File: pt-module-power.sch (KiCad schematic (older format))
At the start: 21 parts, among them U1 MCP16331, U2 MCP16331

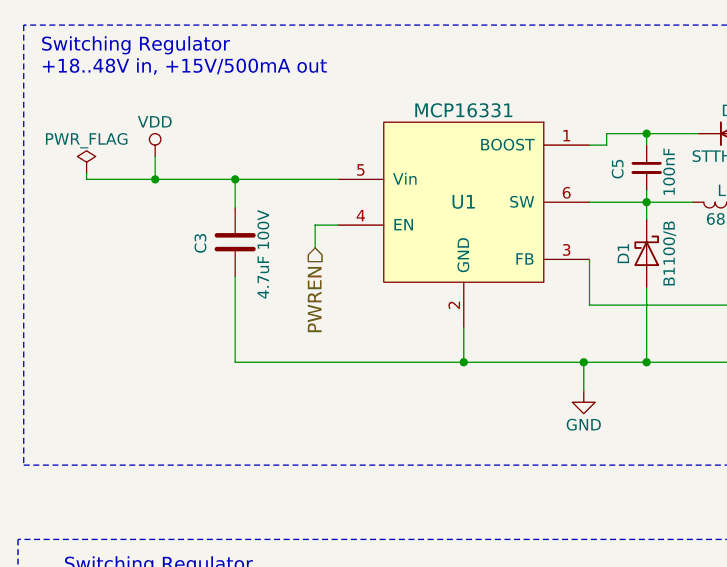
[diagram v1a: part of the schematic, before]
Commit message: Delete pwren
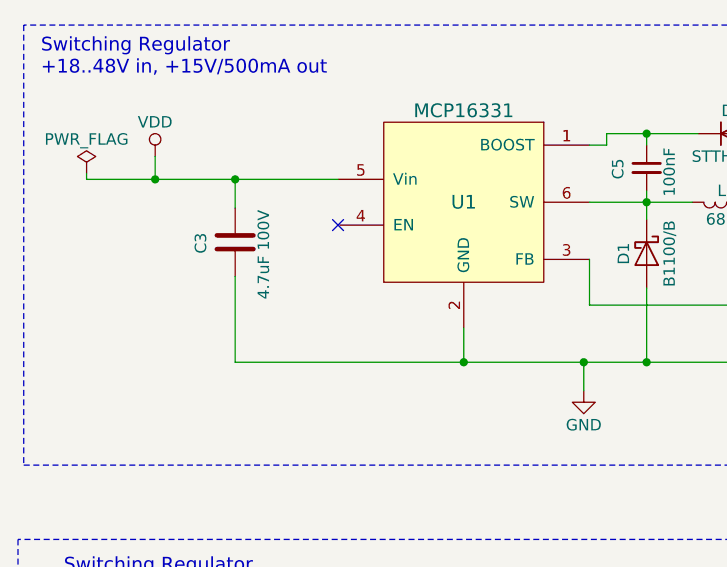
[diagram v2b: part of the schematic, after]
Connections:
- net PWREN: no longer names the net of U1.4 (EN)
- no-connect marks 1 -> 2
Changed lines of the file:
@@
 $EndComp
 $Comp
-L VCC #PWR17
+L VCC #PWR018
 U 1 1 598C3307
 P 3600 4400
-F 0 "#PWR17" H 3600 4250 50  0001 C CNN
+F 0 "#PWR018" H 3600 4250 50  0001 C CNN
 F 1 "VCC" H 3600 4550 50  0000 C CNN
 F 2 "" H 3600 4400 50  0001 C CNN
@@
 $EndComp
 $Comp
-L GND #PWR20
+L GND #PWR019
 U 1 1 598C36A8
 P 4050 4700
-F 0 "#PWR20" H 4050 4450 50  0001 C CNN
+F 0 "#PWR019" H 4050 4450 50  0001 C CNN
 F 1 "GND" H 4050 4550 50  0000 C CNN
 F 2 "" H 4050 4700 50  0001 C CNN
@@
 $EndComp
 $Comp
-L GND #PWR21
+L GND #PWR020
 U 1 1 598C3B7E
 P 5250 5050
-F 0 "#PWR21" H 5250 4800 50  0001 C CNN
+F 0 "#PWR020" H 5250 4800 50  0001 C CNN
 F 1 "GND" H 5250 4900 50  0000 C CNN
 F 2 "" H 5250 5050 50  0001 C CNN
@@
 $EndComp
 $Comp
-L GND #PWR24
+L GND #PWR021
 U 1 1 598C3C64
 P 6550 5500
-F 0 "#PWR24" H 6550 5250 50  0001 C CNN
+F 0 "#PWR021" H 6550 5250 50  0001 C CNN
 F 1 "GND" H 6550 5350 50  0000 C CNN
 F 2 "" H 6550 5500 50  0001 C CNN
@@
 $EndComp
 $Comp
-L GND #PWR23
+L GND #PWR022
 U 1 1 598C5043
 P 6250 4800
-F 0 "#PWR23" H 6250 4550 50  0001 C CNN
+F 0 "#PWR022" H 6250 4550 50  0001 C CNN
 F 1 "GND" H 6250 4650 50  0000 C CNN
 F 2 "" H 6250 4800 50  0001 C CNN
@@
 $EndComp
 $Comp
-L +3.3V #PWR27
+L +3.3V #PWR023
 U 1 1 598C94DC
 P 7500 4600
-F 0 "#PWR27" H 7500 4450 50  0001 C CNN
+F 0 "#PWR023" H 7500 4450 50  0001 C CNN
 F 1 "+3.3V" H 7500 4740 50  0000 C CNN
 F 2 "" H 7500 4600 50  0001 C CNN
@@
 $EndComp
 $Comp
-L PWR_FLAG #FLG5
+L PWR_FLAG #FLG024
 U 1 1 598C9528
 P 7750 4850
-F 0 "#FLG5" H 7750 4925 50  0001 C CNN
+F 0 "#FLG024" H 7750 4925 50  0001 C CNN
 F 1 "PWR_FLAG" H 7750 5000 50  0000 C CNN
 F 2 "" H 7750 4850 50  0001 C CNN
@@
 $EndComp
 $Comp
-L GND #PWR25
+L GND #PWR025
 U 1 1 598CA371
 P 6900 5150
-F 0 "#PWR25" H 6900 4900 50  0001 C CNN
+F 0 "#PWR025" H 6900 4900 50  0001 C CNN
 F 1 "GND" H 6900 5000 50  0000 C CNN
 F 2 "" H 6900 5150 50  0001 C CNN
@@
 $EndComp
 $Comp
-L GND #PWR18
+L GND #PWR026
 U 1 1 598CEACF
 P 3700 4700
-F 0 "#PWR18" H 3700 4450 50  0001 C CNN
+F 0 "#PWR026" H 3700 4450 50  0001 C CNN
 F 1 "GND" H 3700 4550 50  0000 C CNN
 F 2 "" H 3700 4700 50  0001 C CNN
@@
 $EndComp
 $Comp
-L GND #PWR26
+L GND #PWR027
 U 1 1 598CEF8A
 P 7350 5150
-F 0 "#PWR26" H 7350 4900 50  0001 C CNN
+F 0 "#PWR027" H 7350 4900 50  0001 C CNN
 F 1 "GND" H 7350 5000 50  0000 C CNN
 F 2 "" H 7350 5150 50  0001 C CNN
@@
 External_VCC
 $Comp
-L PWR_FLAG #FLG4
+L PWR_FLAG #FLG028
 U 1 1 597BEB38
 P 7725 2225
-F 0 "#FLG4" H 7725 2300 50  0001 C CNN
+F 0 "#FLG028" H 7725 2300 50  0001 C CNN
 F 1 "PWR_FLAG" H 7725 2375 50  0000 C CNN
 F 2 "" H 7725 2225 50  0001 C CNN
@@
 $EndComp
 $Comp
-L GND #PWR22
+L GND #PWR029
 U 1 1 597A23E8
 P 5675 3100
-F 0 "#PWR22" H 5675 2850 50  0001 C CNN
+F 0 "#PWR029" H 5675 2850 50  0001 C CNN
 F 1 "GND" H 5675 2950 50  0000 C CNN
 F 2 "" H 5675 3100 50  0001 C CNN
@@
 	0    1    1    0
 $EndComp
-Wire Wire Line
-	4500 2375 4600 2375
-Wire Wire Line
-	4500 2475 4500 2375
 Wire Notes Line
 	8025 1500 3225 1500
@@
 Text Notes 3300 1725 0    60   ~ 0
 Switching Regulator\n+18..48V in, +15V/500mA out
-Text HLabel 4500 2475 3    60   Input ~ 0
-PWREN
 $Comp
 L MCP16331 U1
@@
 $EndComp
 $Comp
-L VDD #PWR19
+L VDD #PWR030
 U 1 1 597A11B1
 P 3800 2075
-F 0 "#PWR19" H 3800 1925 50  0001 C CNN
+F 0 "#PWR030" H 3800 1925 50  0001 C CNN
 F 1 "VDD" H 3800 2225 50  0000 C CNN
 F 2 "" H 3800 2075 50  0001 C CNN
@@
 $EndComp
 $Comp
-L PWR_FLAG #FLG3
+L PWR_FLAG #FLG031
 U 1 1 59948AC3
 P 3500 2150
-F 0 "#FLG3" H 3500 2225 50  0001 C CNN
+F 0 "#FLG031" H 3500 2225 50  0001 C CNN
 F 1 "PWR_FLAG" H 3500 2300 50  0000 C CNN
 F 2 "" H 3500 2150 50  0001 C CNN
@@
 Connection ~ 3800 2175
 $Comp
-L PWR_FLAG #FLG2
+L PWR_FLAG #FLG032
 U 1 1 59958159
 P 3475 4400
-F 0 "#FLG2" H 3475 4475 50  0001 C CNN
+F 0 "#FLG032" H 3475 4475 50  0001 C CNN
 F 1 "PWR_FLAG" H 3475 4550 50  0000 C CNN
 F 2 "" H 3475 4400 50  0001 C CNN
@@
 $EndComp
 Connection ~ 3600 4400
+NoConn ~ 4600 2375
 $EndSCHEMATC

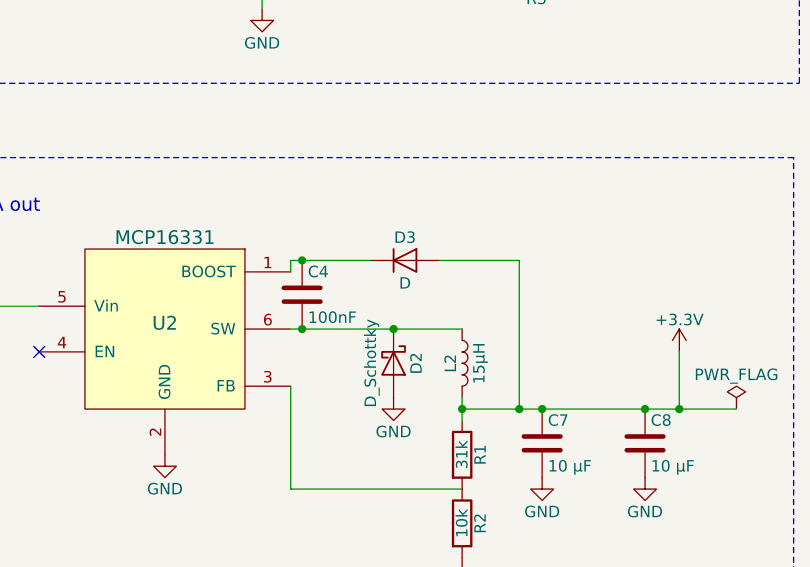
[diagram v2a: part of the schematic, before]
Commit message: add all the rest of the footprints
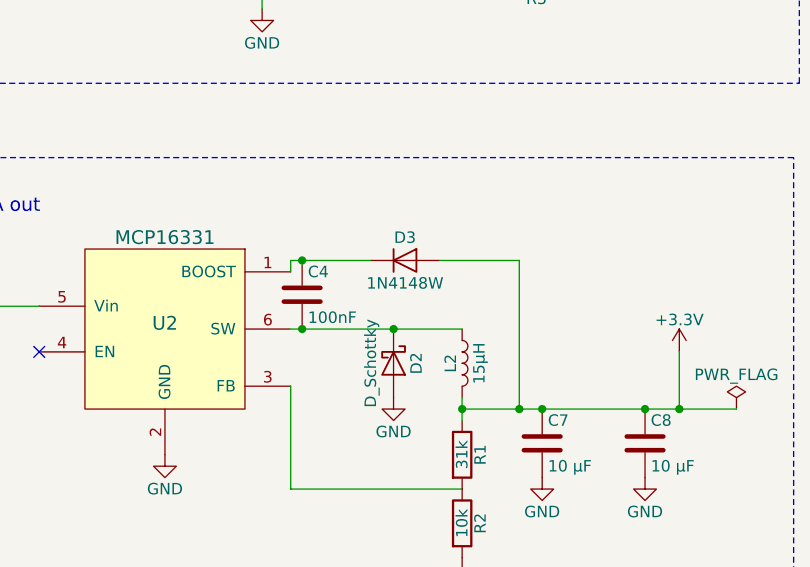
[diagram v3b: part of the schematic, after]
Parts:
- C1, C2, C3, C4, C5, C6, C7, C8: footprint (none) -> Capacitors_SMD:C_1206_HandSoldering
- D2: footprint (none) -> Diodes_SMD:D_SMA
- D3: value D -> 1N4148W; footprint (none) -> Diodes_SMD:D_SOD-123F
- L2: footprint (none) -> .pretty:SM-4.3x4.3
- R1, R2, R3, R4: footprint (none) -> Resistors_SMD:R_1206_HandSoldering
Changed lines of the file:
@@
 F 0 "C2" H 4075 4650 50  0000 L CNN
 F 1 "10 µF" H 4075 4450 50  0000 L CNN
-F 2 "" H 4088 4400 50  0001 C CNN
+F 2 "Capacitors_SMD:C_1206_HandSoldering" H 4088 4400 50  0001 C CNN
 F 3 "" H 4050 4550 50  0001 C CNN
 	1    4050 4550
@@
 F 0 "R2" V 6630 5350 50  0000 C CNN
 F 1 "10k" V 6550 5350 50  0000 C CNN
-F 2 "" V 6480 5350 50  0001 C CNN
+F 2 "Resistors_SMD:R_1206_HandSoldering" V 6480 5350 50  0001 C CNN
 F 3 "" H 6550 5350 50  0001 C CNN
 	1    6550 5350
@@
 F 0 "R1" V 6630 5050 50  0000 C CNN
 F 1 "31k" V 6550 5050 50  0000 C CNN
-F 2 "" V 6480 5050 50  0001 C CNN
+F 2 "Resistors_SMD:R_1206_HandSoldering" V 6480 5050 50  0001 C CNN
 F 3 "" H 6550 5050 50  0001 C CNN
 	1    6550 5050
@@
 F 0 "D2" H 6250 4750 50  0000 C CNN
 F 1 "D_Schottky" H 6250 4550 50  0000 C CNN
-F 2 "" H 6250 4650 50  0001 C CNN
+F 2 "Diodes_SMD:D_SMA" H 6250 4650 50  0001 C CNN
 F 3 "" H 6250 4650 50  0001 C CNN
 	1    6250 4650
@@
 F 0 "L2" V 6500 4650 50  0000 C CNN
 F 1 "15µH" V 6625 4650 50  0000 C CNN
-F 2 "" H 6550 4650 50  0001 C CNN
+F 2 ".pretty:SM-4.3x4.3" H 6550 4650 50  0001 C CNN
 F 3 "" H 6550 4650 50  0001 C CNN
 	1    6550 4650
@@
 F 0 "C4" H 5875 4450 50  0000 L CNN
 F 1 "100nF" H 5875 4250 50  0000 L CNN
-F 2 "" H 5888 4200 50  0001 C CNN
+F 2 "Capacitors_SMD:C_1206_HandSoldering" H 5888 4200 50  0001 C CNN
 F 3 "" H 5850 4350 50  0001 C CNN
 	1    5850 4350
@@
 P 6300 4200
 F 0 "D3" H 6300 4300 50  0000 C CNN
-F 1 "D" H 6300 4100 50  0000 C CNN
-F 2 "" H 6300 4200 50  0001 C CNN
+F 1 "1N4148W" H 6300 4100 50  0000 C CNN
+F 2 "Diodes_SMD:D_SOD-123F" H 6300 4200 50  0001 C CNN
 F 3 "" H 6300 4200 50  0001 C CNN
 	1    6300 4200
@@
 F 0 "C7" H 6925 5100 50  0000 L CNN
 F 1 "10 µF" H 6925 4900 50  0000 L CNN
-F 2 "" H 6938 4850 50  0001 C CNN
+F 2 "Capacitors_SMD:C_1206_HandSoldering" H 6938 4850 50  0001 C CNN
 F 3 "" H 6900 5000 50  0001 C CNN
 	1    6900 5000
@@
 F 0 "C1" H 3725 4650 50  0000 L CNN
 F 1 "10 µF" H 3725 4450 50  0000 L CNN
-F 2 "" H 3738 4400 50  0001 C CNN
+F 2 "Capacitors_SMD:C_1206_HandSoldering" H 3738 4400 50  0001 C CNN
 F 3 "" H 3700 4550 50  0001 C CNN
 	1    3700 4550
@@
 F 0 "C8" H 7375 5100 50  0000 L CNN
 F 1 "10 µF" H 7375 4900 50  0000 L CNN
-F 2 "" H 7388 4850 50  0001 C CNN
+F 2 "Capacitors_SMD:C_1206_HandSoldering" H 7388 4850 50  0001 C CNN
 F 3 "" H 7350 5000 50  0001 C CNN
 	1    7350 5000
@@
 F 0 "C6" V 6500 2475 50  0000 L CNN
 F 1 "22uF 25V" V 6775 2350 50  0000 L CNN
-F 2 "" H 6688 2375 50  0001 C CNN
+F 2 "Capacitors_SMD:C_1206_HandSoldering" H 6688 2375 50  0001 C CNN
 F 3 "" H 6650 2525 50  0001 C CNN
 	1    6650 2525
@@
 F 0 "R3" V 6955 2975 50  0000 C CNN
 F 1 "6.2k" V 6875 2975 50  0000 C CNN
-F 2 "" V 6805 2975 50  0001 C CNN
+F 2 "Resistors_SMD:R_1206_HandSoldering" V 6805 2975 50  0001 C CNN
 F 3 "" H 6875 2975 50  0001 C CNN
 	1    6875 2975
@@
 F 0 "R4" V 7180 2500 50  0000 C CNN
 F 1 "110k" V 7100 2500 50  0000 C CNN
-F 2 "" V 7030 2500 50  0001 C CNN
+F 2 "Resistors_SMD:R_1206_HandSoldering" V 7030 2500 50  0001 C CNN
 F 3 "" H 7100 2500 50  0001 C CNN
 	1    7100 2500
@@
 F 0 "C5" V 5825 2075 50  0000 L CNN
 F 1 "100nF" V 6050 2000 50  0000 L CNN
-F 2 "" H 5950 2125 50  0001 C CNN
+F 2 "Capacitors_SMD:C_1206_HandSoldering" H 5950 2125 50  0001 C CNN
 F 3 "" H 5950 2125 50  0001 C CNN
 	1    5950 2125
@@
 Switching Regulator\n+18..48V in, +15V/500mA out
 $Comp
-L MCP16331 U1
-U 1 1 597A1586
-P 5150 2275
-F 0 "U1" H 5150 2275 60  0000 C CNN
-F 1 "MCP16331" H 5150 2675 60  0000 C CNN
-F 2 "TO_SOT_Packages_SMD:SOT-23-6" H 5150 2125 60  0001 C CNN
-F 3 "" H 5150 2125 60  0001 C CNN
-	1    5150 2275
-	1    0    0    -1
-$EndComp
-$Comp
 L VDD #PWR030
 U 1 1 597A11B1
@@
 F 0 "C3" V 4000 2400 50  0000 L CNN
 F 1 "4.7uF 100V" V 4275 2200 50  0000 L CNN
-F 2 "" H 4188 2300 50  0001 C CNN
+F 2 "Capacitors_SMD:C_1206_HandSoldering" H 4188 2300 50  0001 C CNN
 F 3 "" H 4150 2450 50  0001 C CNN
 	1    4150 2450
@@
 $EndComp
 Connection ~ 3600 4400
+$Comp
+L MCP16331 U1
+U 1 1 597A1586
+P 5150 2275
+F 0 "U1" H 5150 2275 60  0000 C CNN
+F 1 "MCP16331" H 5150 2675 60  0000 C CNN
+F 2 "TO_SOT_Packages_SMD:SOT-23-6" H 5150 2125 60  0001 C CNN
+F 3 "" H 5150 2125 60  0001 C CNN
+	1    5150 2275
+	1    0    0    -1
+$EndComp
 NoConn ~ 4600 2375
 $EndSCHEMATC
